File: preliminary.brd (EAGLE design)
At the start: 79.5 x 77.5 mm, 64 parts, among them IC1 STM32F407VGT6, J3 POWER_JACK, Q1 600mA/40V, U1 STMPS2141STR, U2 3.3V, Y1 8MHz

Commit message: Schematic changed
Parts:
- removed D2: SFH482, led:SFH482
- removed D5: BLUE, SparkFun-LED:LED-0603
- removed S2: (no value), SparkFun-Switches:TACTILE_SWITCH_SMD_4.6X2.8MM
- removed U2: 3.3V, SparkFun-IC-Power:SOT23-5
- added C25, C26, C27: 47uF, SparkFun-Capacitors:1206
- added C28: 10uF, SparkFun-Capacitors:0603
- added D6: SFH482, led:SFH482
- added D7: BLUE, SparkFun-LED:LED-0603
- added J4: (no value), SparkFun-Connectors:1X02
- added R22: 0, SparkFun-Resistors:0603
- added U$4: TPSM5, preliminary:TO-220
- added U$5: TPSM3.3, preliminary:TO-220
- C23: value 1uF -> 10uF
- C24: value 1uF -> 47uF; device SparkFun-Capacitors:0603 -> SparkFun-Capacitors:1206
- D1: value SFH482 -> BLUE; device led:SFH482 -> SparkFun-LED:LED-0603
- D3, D4: value BLUE -> SFH482; device SparkFun-LED:LED-0603 -> led:SFH482
- moved D1 103.3 mm to (1.60, -29.3)
- moved C24 101.8 mm to (-2.40, -49.2), turned to 0 degrees
- moved C23 100.0 mm to (2.80, -50.7), turned to 0 degrees
- moved D4 62.4 mm to (8.00, -21.0)
- moved D3 46.4 mm to (8.00, -7.70)
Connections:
- removed net 3V: C24.2, U2.5
- removed net 5V: C23.2, J3.PWR, U2.1, U2.3
- removed net VDD: C10.1, C11.1, C12.1, C13.1, C17.1, C18.1, C6.1, C7.1, C8.1, C9.1, IC1.100, IC1.11, IC1.19, IC1.28, IC1.50, IC1.75, MK1.1, MK1.2, MK1.5, R11.2, R13.2, R16.1, R17.1, R5.2, R6.1, R7.1, S2.1, S2.2, U$1.1, U$2.CH_PD, U$2.RST, U$2.VCC, U1.5
- new net +3V3: C10.1, C11.1, C12.1, C13.1, C17.1, C18.1, C26.1, C27.1, C6.1, C7.1, C8.1, C9.1, IC1.100, IC1.11, IC1.19, IC1.28, IC1.50, IC1.75, J4.1, MK1.1, MK1.2, MK1.5, R11.2, R13.2, R16.1, R17.1, R5.2, R6.1, R7.1, U$1.1, U$2.CH_PD, U$2.RST, U$2.VCC, U$5.P$3
- new net +5V: C24.1, C25.1, C28.1, U$4.P$3, U1.5
- new net N$23: C23.1, J3.PWR, U$4.P$1
- new net N$25: IC1.94, R22.2
- net GND: now also C23.2, C24.2, C25.2, C26.2, C27.2, C28.2, D6.K, R22.1, U$4.P$2, U$5.P$2; no longer C23.1, C24.1, D3.C, D4.C, D5.C, IC1.94, U2.2
- net N$10: now also D1.A; no longer D2.A
- net N$11: now also D6.A; no longer D3.A
- net N$17: no longer D4.A
- net N$18: no longer D5.A
- net N$4: now also J4.2; no longer S2.3, S2.4
- net N$5: now also D7.A; no longer D1.A
- net N$9: now also D1.C; no longer D2.K
- net PD5: now also D7.C; no longer D1.K
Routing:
- net VDD: track 373.6 -> 0.00 mm, vias 7 -> 0
- net +3V3: track 0.00 -> 368.4 mm, vias 0 -> 7
- net 5V: track 21.3 -> 0.00 mm
- net GND: track 469.3 -> 454.6 mm
- net N$10: track 11.9 -> 0.00 mm
- net N$9: track 9.24 -> 0.00 mm
- net 3V: track 8.25 -> 0.00 mm
- net PD5: track 14.2 -> 12.5 mm
- net N$4: track 20.4 -> 19.9 mm

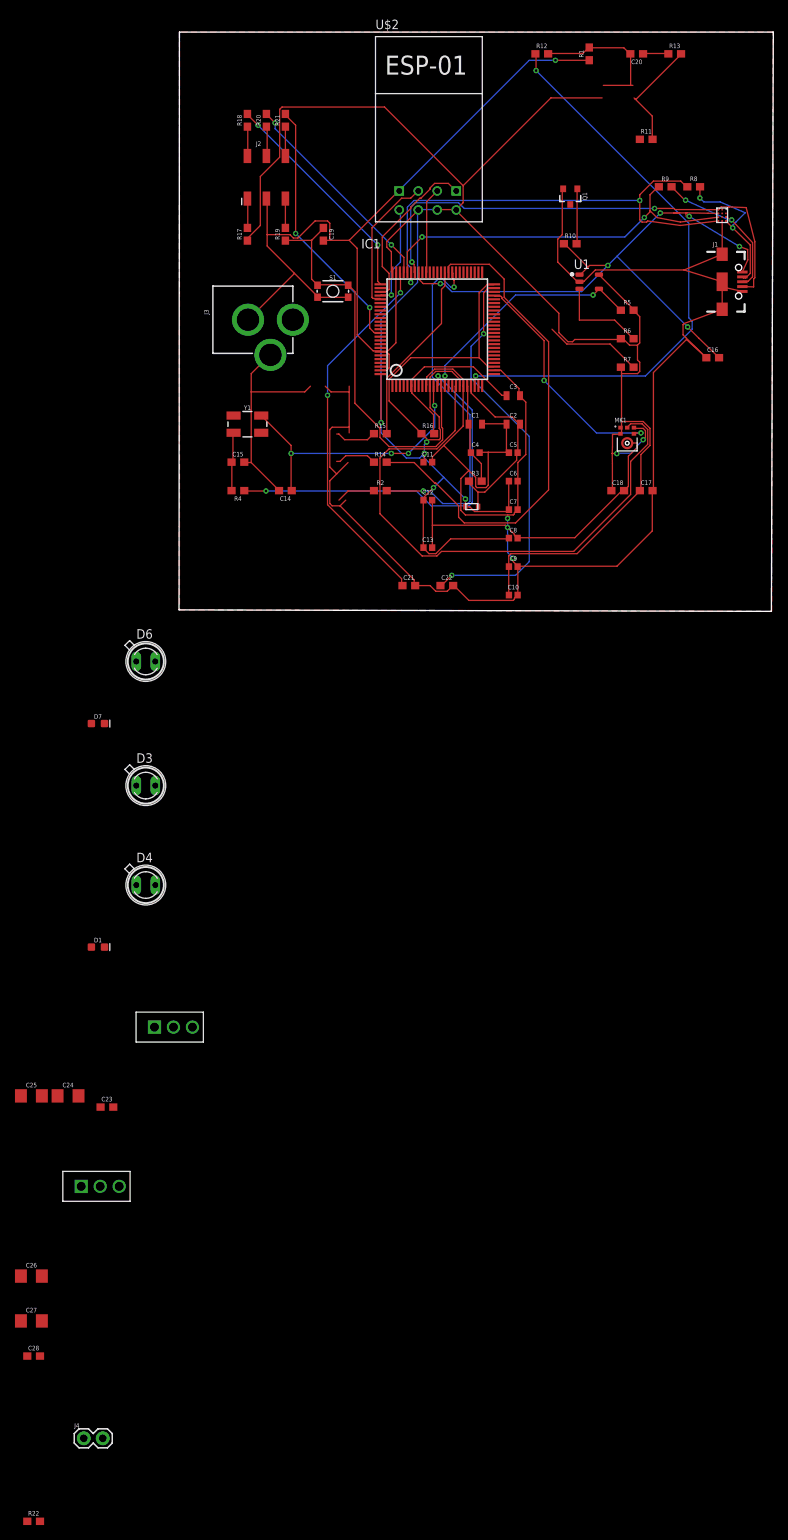
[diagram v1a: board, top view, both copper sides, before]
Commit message: Placing components on the PCB
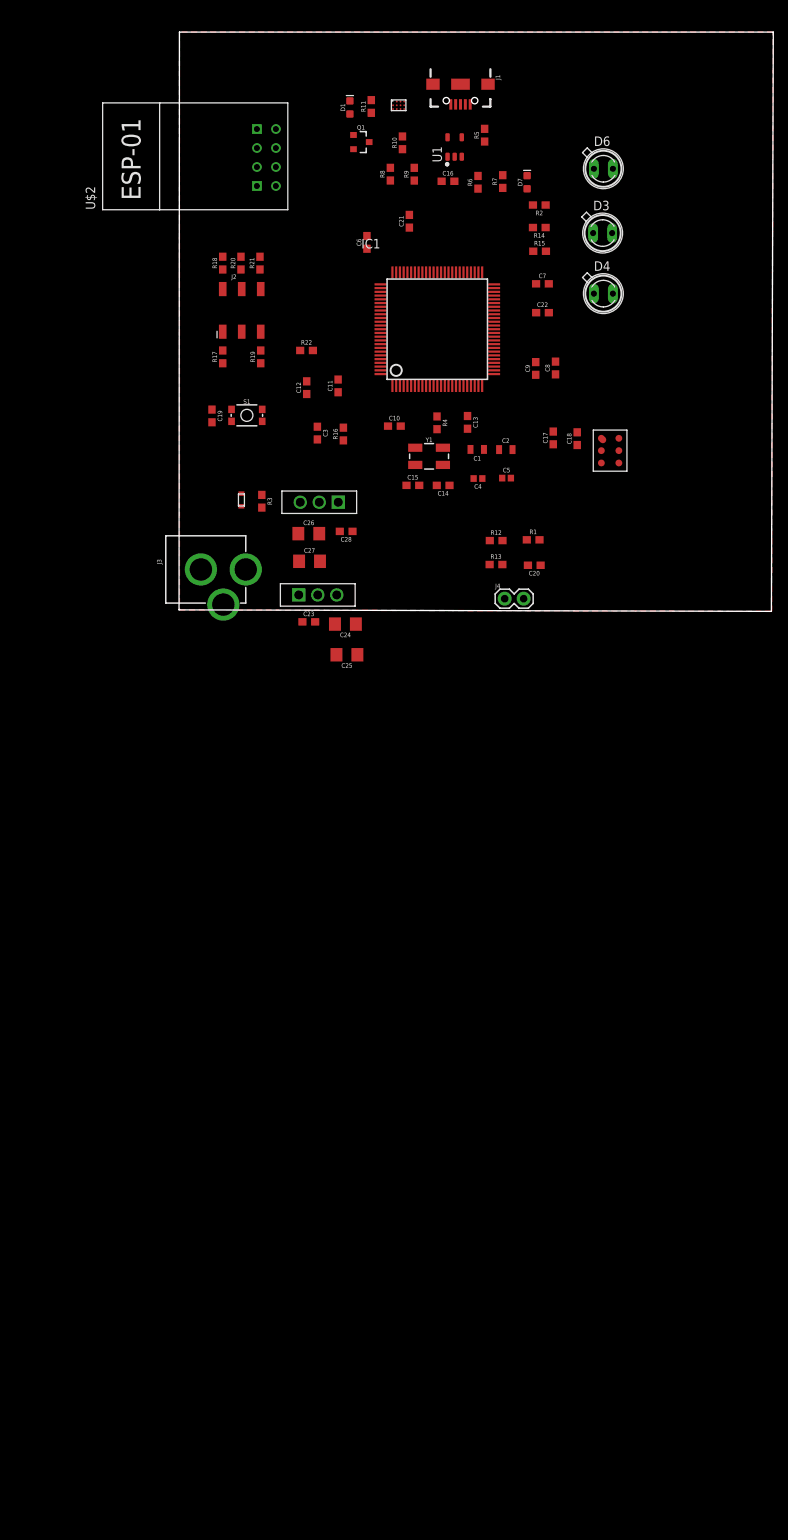
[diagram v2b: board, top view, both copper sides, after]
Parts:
- removed MK1: SPH0645LM4H-B, SPH0645LM4H-B:MIC_SPH0645LM4H-B
- added U$6: MP45DT02-M, preliminary:HLGA
- C10, C11, C12, C13, C6, C7, C8, C9: device SparkFun-Capacitors:0402 -> SparkFun-Capacitors:0603
- C17: value 0.1uF -> 100nF
- C18: value 200pF -> 10uF
- C3: value 1.0uF -> 100nF; device SparkFun-Capacitors:0805 -> SparkFun-Capacitors:0603
- moved R22 160.8 mm to (29.5, 50.5)
- moved J4 125.6 mm to (56.0, 17.3)
- moved C28 118.0 mm to (34.8, 26.3), turned to 180 degrees
- moved D1 117.2 mm to (35.3, 83.0), turned to 90 degrees
- moved C27 108.2 mm to (29.9, 22.3)
- moved C26 106.0 mm to (29.8, 26.0)
- moved D4 100.0 mm to (69.2, 58.1)
- moved U$5 96.1 mm to (31.2, 30.2), turned to 180 degrees
- moved D3 95.9 mm to (69.1, 66.2)
- moved D7 92.4 mm to (59.0, 73.0), turned to 90 degrees
- moved D6 89.9 mm to (69.2, 74.8)
- moved C24 73.2 mm to (34.7, 13.9), turned to 180 degrees
- moved C25 72.5 mm to (34.9, 9.80), turned to 180 degrees
- moved R13 72.4 mm to (54.8, 21.9)
- moved C23 70.3 mm to (29.8, 14.2)
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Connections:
- new net VDD: C17.1, C18.1, U$6.VDD1, U$6.VDD2
- net +3V3: no longer C17.1, C18.1, MK1.1, MK1.2, MK1.5
- net GND: now also D3.K, D4.K, U$6.GND1, U$6.GND2, U$6.LR; no longer MK1.3
- net N$17: now also D3.A
- net N$18: now also D4.A
- net PB10: now also U$6.CLK; no longer MK1.4
- net PC3: now also U$6.DOUT; no longer MK1.6
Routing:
- net GND: track 454.6 -> 0.00 mm, vias 4 -> 0
- net +3V3: track 368.4 -> 0.00 mm, vias 7 -> 0
- net PA9: track 88.0 -> 0.00 mm, vias 6 -> 0
- net PA0: track 78.5 -> 0.00 mm, vias 2 -> 0
- net PC3: track 77.3 -> 0.00 mm
- net N$14: track 67.6 -> 0.00 mm
- net PA10: track 67.0 -> 0.00 mm, vias 2 -> 0
- net PA11: track 64.7 -> 0.00 mm, vias 2 -> 0
- net NRST: track 55.0 -> 0.00 mm
- net N$20: track 54.7 -> 0.00 mm, vias 2 -> 0
- net N$1: track 51.7 -> 0.00 mm, vias 2 -> 0
- net PA12: track 51.0 -> 0.00 mm, vias 2 -> 0
- net N$19: track 50.2 -> 0.00 mm, vias 2 -> 0
- net N$16: track 48.7 -> 0.00 mm, vias 2 -> 0
- net N$3: track 38.0 -> 0.00 mm, vias 4 -> 0
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
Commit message: 2nd revision finished
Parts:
- removed J1: (no value), SparkFun-Connectors:USB-AB-MICRO-SMD
- removed U$3: EMIF02-USB03F2, EMIF02-USB03F2:FLIP-CHIP
- added H1, H2, H3, H4: STAND-OFF, SparkFun-Hardware:STAND-OFF
- added J5: (no value), SparkFun-Connectors:USB-MICROB
- moved D1 37.1 mm to (63.9, 59.3), flipped to the bottom, turned to 270 degrees
- moved R11 31.3 mm to (62.1, 62.9), flipped to the bottom, turned to 0 degrees
- moved Q1 30.2 mm to (60.2, 59.2), flipped to the bottom, turned to 90 degrees
- moved D7 26.2 mm to (38.6, 56.6), flipped to the bottom
- moved R7 22.3 mm to (40.9, 56.4), flipped to the bottom, turned to 270 degrees
- moved R5 21.7 mm to (34.9, 67.8), flipped to the bottom, turned to 270 degrees
- moved R10 19.9 mm to (55.5, 63.3), flipped to the bottom, turned to 270 degrees
- moved R6 18.6 mm to (43.9, 56.5), flipped to the bottom
- moved U$2 18.3 mm to (30.7, 64.0), turned to 0 degrees
- moved C16 16.7 mm to (46.9, 56.5), flipped to the bottom, turned to 90 degrees
- moved R2 14.7 mm to (61.3, 55.2), flipped to the bottom, turned to 0 degrees
- moved R14 14.7 mm to (61.3, 52.2), flipped to the bottom, turned to 0 degrees
- moved R15 14.7 mm to (61.2, 49.1), flipped to the bottom
- moved U1 14.3 mm to (39.5, 67.3), flipped to the bottom
- moved D6 14.1 mm to (68.5, 60.7), flipped to the bottom, turned to 270 degrees
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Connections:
- removed net VDD: C17.1, C18.1, U$6.VDD1, U$6.VDD2
- net +3V3: now also C17.1, C18.1, U$6.VDD1, U$6.VDD2
- net +5V: now also U$5.P$1
- net GND: now also J5.GND; no longer J1.GND1, J1.SHLD1, J1.SHLD2, J1.SHLD3, U$3.11
- net N$6: now also J5.D-; no longer J1.D-1, U$3.10
- net N$7: now also J5.D+; no longer J1.D+1, U$3.7
- net PA10: now also J5.ID; no longer J1.ID1, U$3.3
- net PA11: no longer U$3.12
- net PA12: no longer U$3.9
- net PA9: now also J5.VBUS; no longer J1.VBUS1, U$3.6
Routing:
- net +3V3: track 0.00 -> 230.3 mm, vias 0 -> 22
- net +5V: track 0.00 -> 95.9 mm, vias 0 -> 3
- net PC0: track 0.00 -> 52.9 mm, vias 0 -> 3
- net VDDA: track 0.00 -> 50.9 mm, vias 0 -> 3
- net PA9: track 0.00 -> 40.3 mm, vias 0 -> 1
- net NRST: track 0.00 -> 38.7 mm, vias 0 -> 2
- net VREF+: track 0.00 -> 38.2 mm, vias 0 -> 2
- net PB10: track 0.00 -> 30.3 mm, vias 0 -> 2
- net PA13: track 0.00 -> 28.3 mm, vias 0 -> 2
- net PA14: track 0.00 -> 25.9 mm, vias 0 -> 2
- net N$23: track 0.00 -> 25.7 mm
- net PC3: track 0.00 -> 24.7 mm, vias 0 -> 2
- net PA0: track 0.00 -> 21.6 mm, vias 0 -> 2
- net PB3: track 0.00 -> 21.3 mm
- net N$13: track 0.00 -> 19.5 mm, vias 0 -> 3
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- added copper zone on layer 16, net GND
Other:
- board size 79.5 x 77.5 mm -> 61 x 59 mm
